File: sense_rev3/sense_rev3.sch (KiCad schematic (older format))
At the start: 43 parts, among them J1 Audio-Jack-4, P1 CONN_02X05, Q1 TSM2301, SW1 SW_SPST, U1 TLV8802, U2 MDBT42Q, U3 PIR, Y1 Crystal

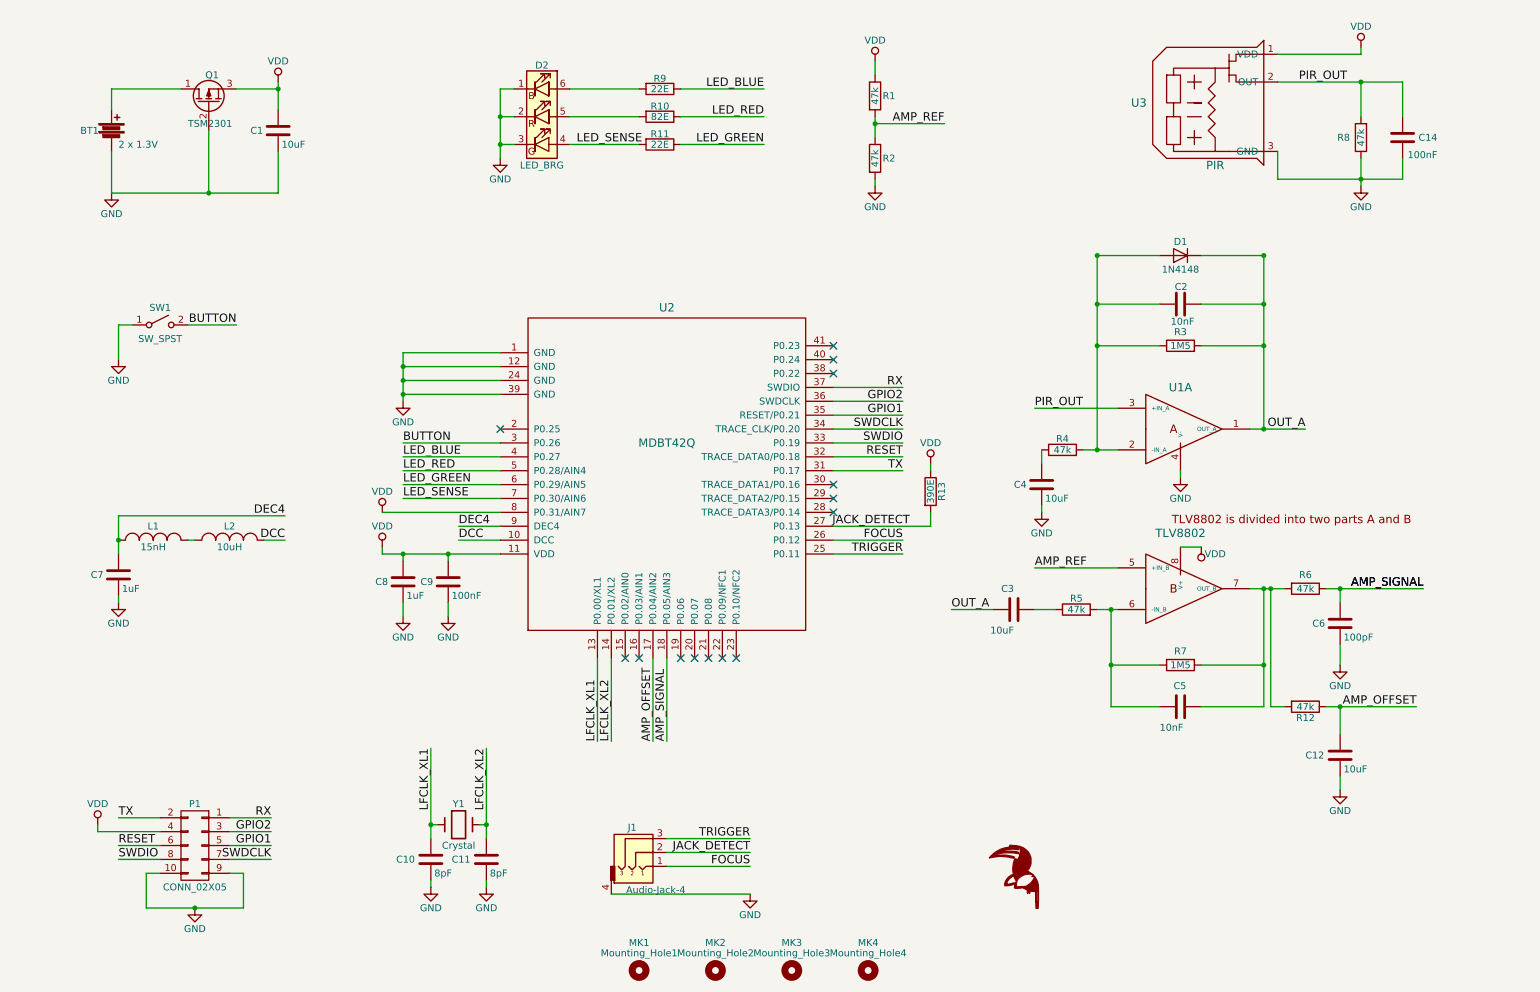
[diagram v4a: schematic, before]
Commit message: Adds new datasheets & schematics
-D204B PIR
-KP506B PIR
-T38G-32_768K12 Crystal
-G366 enclosure
-Sense_rev3 schematics files: with comments and explainations.
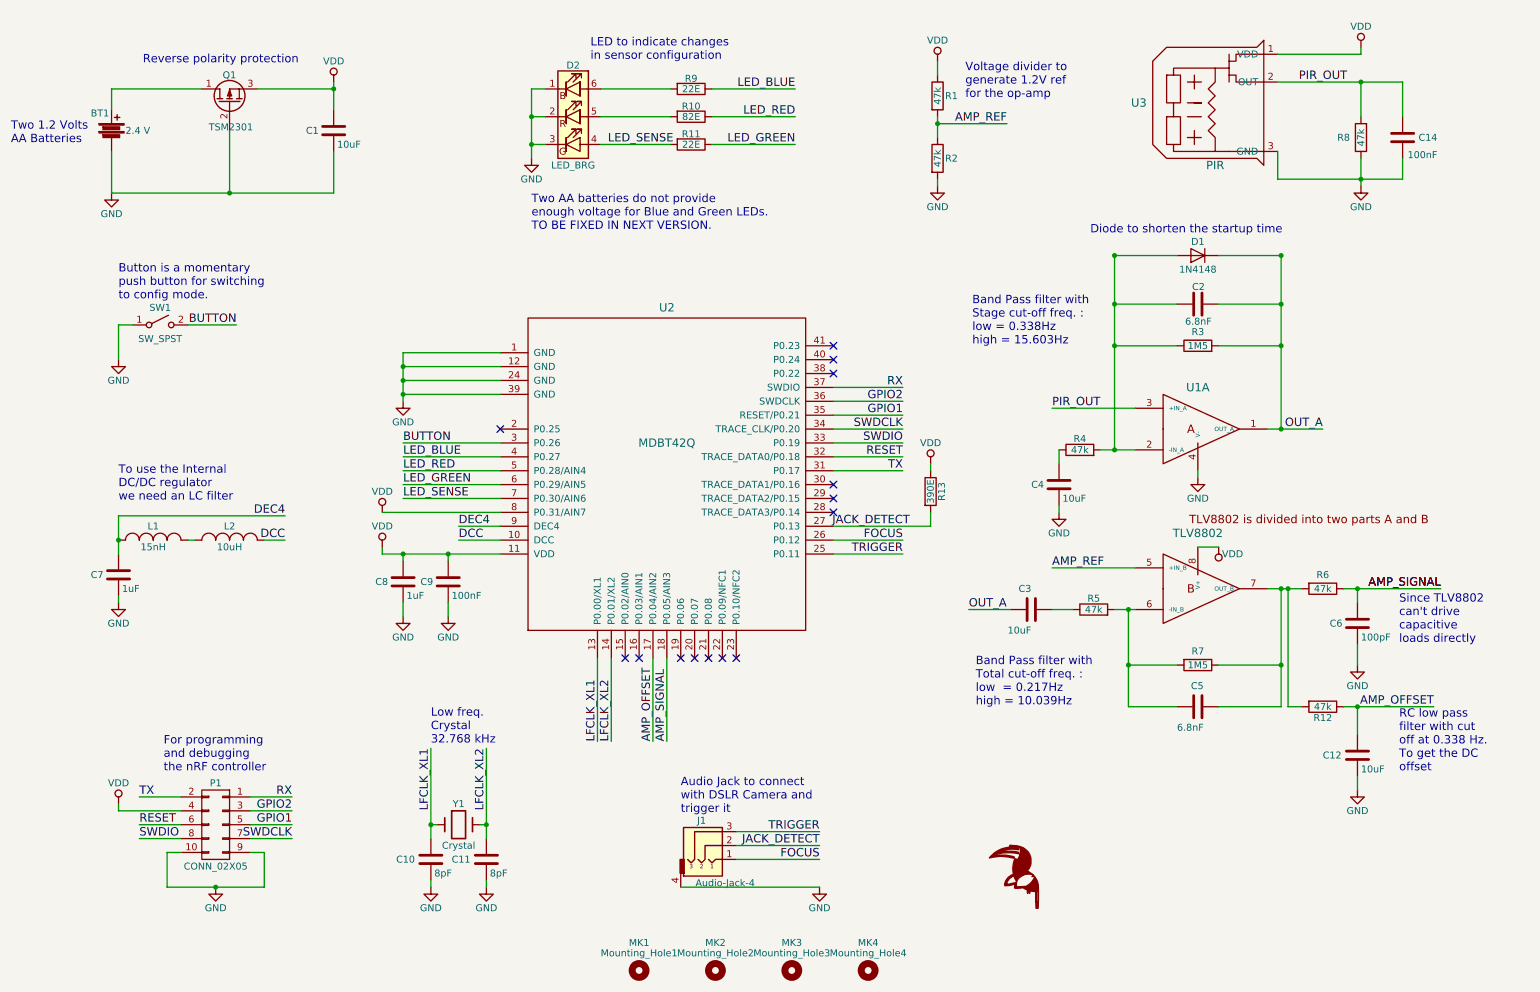
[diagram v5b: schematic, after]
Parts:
- BT1: value 2 x 1.3V -> 2.4 V
- C2, C5: value 10nF -> 6.8nF
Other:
- note added: "Audio Jack to connect\nwith DSLR Camera and\ntrigger it"
- note added: "Band Pass filter with\nStage cut-off freq. :\nlow = 0.338Hz\nhigh = 15.603Hz"
- note added: "Band Pass filter with\nTotal cut-off freq. :\nlow = 0.217Hz\nhigh = 10.039Hz"
- note added: "Button is a momentary\npush button for switching\nto config mode."
- note added: "Diode to shorten the startup time"
- note added: "For programming\nand debugging\nthe nRF controller"
- note added: "LED to indicate changes\nin sensor configuration\n"
- note added: "Low freq.\nCrystal\n32.768 kHz"
- note added: "RC low pass\nfilter with cut\noff at 0.338 Hz.\nTo get the DC\noffset"
- note added: "Reverse polarity protection"
- note added: "Since TLV8802\ncan't drive\ncapacitive \nloads directly"
- note added: "To use the Internal\nDC/DC regulator\nwe need an LC filter"
- note added: "Two 1.2 Volts\nAA Batteries"
- note added: "Two AA batteries do not provide\nenough voltage for Blue and Green LEDs.\nTO BE FIXED IN NEXT VERSION."
- note added: "Voltage divider to\ngenerate 1.2V ref\nfor the op-amp"
- moved on the sheet: C1, C12, C2, C3, C4, C5, C6, D1, D2, J1, P1, Q1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
